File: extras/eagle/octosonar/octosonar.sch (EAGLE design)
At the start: 21 parts, among them IC1 PCF8574TW, IC2 74HC125D, IC3 74HC125D

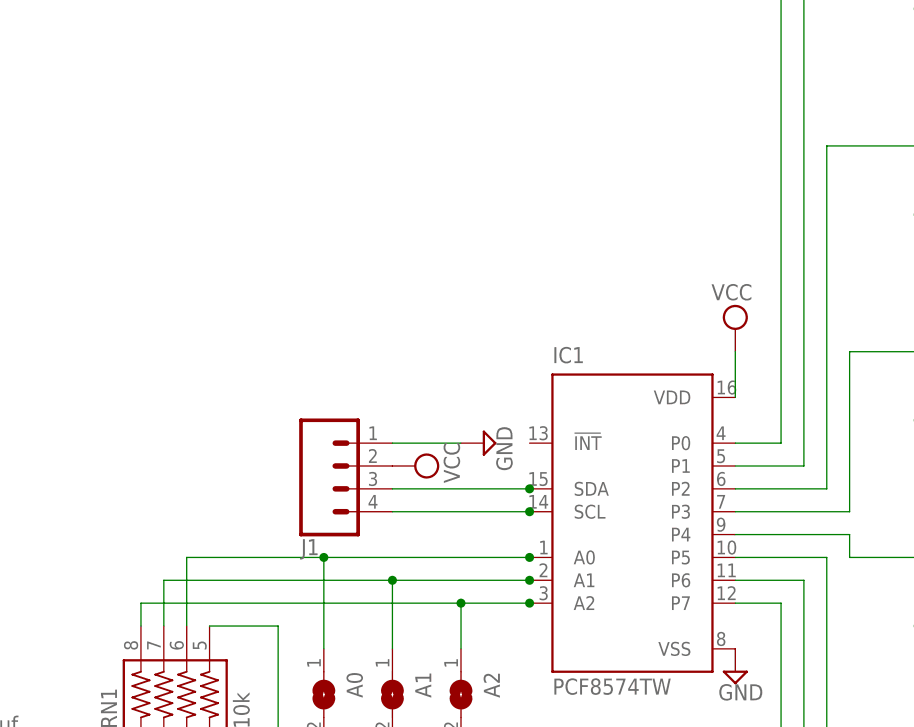
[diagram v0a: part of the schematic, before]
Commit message: octosonar board 2.1 first pass
input pins on grid
add i2c pullups
silkscreen rework
full re-route
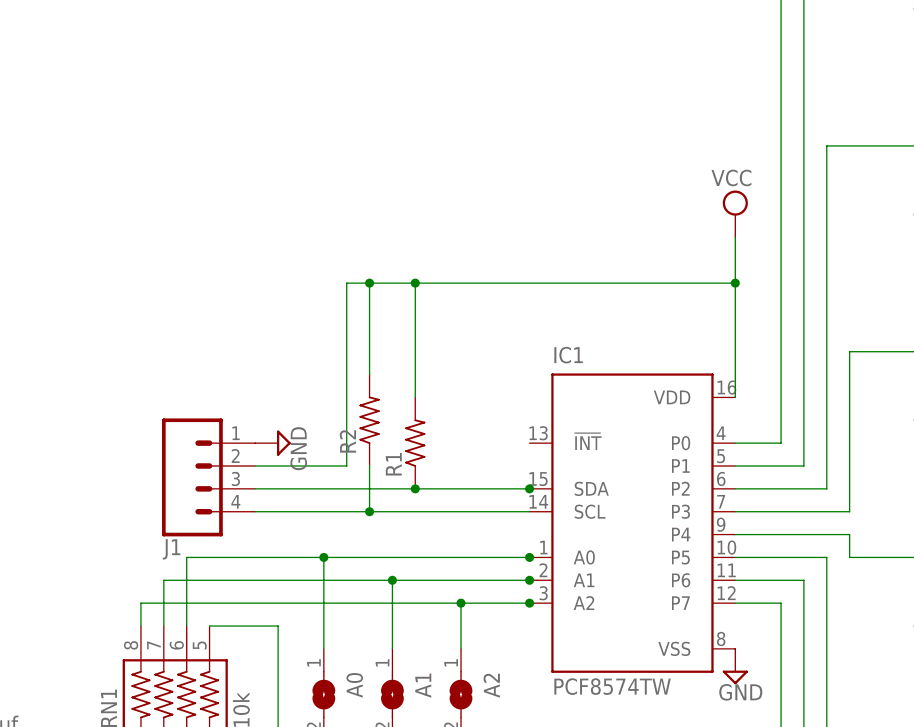
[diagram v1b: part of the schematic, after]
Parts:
- added R1, R2: (no value), rcl:R-US_0204/2V
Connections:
- net N$21: now also R2.1
- net N$22: now also R1.1
- net VCC: now also R1.2, R2.2
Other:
- moved on the sheet: J1
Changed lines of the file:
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@@
 <?xml version="1.0" encoding="utf-8"?>
 <!DOCTYPE eagle SYSTEM "eagle.dtd">
-<eagle version="8.2.0">
+<eagle version="8.2.1">
 <drawing>
 <settings>
@@
 <layers>
 <layer number="1" name="Top" color="4" fill="1" visible="no" active="no"/>
+<layer number="2" name="Route2" color="1" fill="3" visible="no" active="no"/>
+<layer number="15" name="Route15" color="4" fill="6" visible="no" active="no"/>
 <layer number="16" name="Bottom" color="1" fill="1" visible="no" active="no"/>
 <layer number="17" name="Pads" color="2" fill="1" visible="no" active="no"/>
@@
 <parts>
 <part name="IC2" library="74xx-eu" deviceset="74*125" device="D" technology="HC"/>
-<part name="IC3" library="74xx-eu" deviceset="74*125" device="D" technology="HC"/>
+<part name="IC3" library="74xx-eu" library_urn="urn:adsk.eagle:library:85" deviceset="74*125" device="D" technology="HC"/>
 <part name="S0" library="SparkFun-Connectors" deviceset="CONN_04" device="POLAR_LOCK" value="0"/>
 <part name="S1" library="SparkFun-Connectors" deviceset="CONN_04" device="POLAR_LOCK" value="1"/>
@@
 <part name="SUPPLY18" library="supply2" deviceset="VCC" device=""/>
 <part name="J1" library="SparkFun-Connectors" deviceset="CONN_04" device="POLAR_LOCK"/>
-<part name="SUPPLY21" library="supply2" deviceset="VCC" device=""/>
 <part name="SUPPLY22" library="supply2" deviceset="GND" device=""/>
 <part name="J2" library="SparkFun-Connectors" deviceset="CONN_02" device="POLAR_LOCK"/>
@@
 <part name="VCC1" library="supply2" deviceset="VCC" device=""/>
 <part name="SUPPLY25" library="supply2" deviceset="GND" device=""/>
+<part name="R1" library="rcl" library_urn="urn:adsk.eagle:library:334" deviceset="R-US_" device="0204/2V"/>
+<part name="R2" library="rcl" library_urn="urn:adsk.eagle:library:334" deviceset="R-US_" device="0204/2V"/>
 </parts>
 <sheets>
@@
 <instance part="SUPPLY14" gate="GND" x="111.76" y="-101.6"/>
 <instance part="SUPPLY18" gate="G$1" x="5.08" y="-55.88" rot="R180"/>
-<instance part="J1" gate="G$1" x="0" y="-10.16" rot="MR180"/>
-<instance part="SUPPLY21" gate="G$1" x="7.62" y="-10.16" rot="MR90"/>
-<instance part="SUPPLY22" gate="GND" x="15.24" y="-7.62" rot="MR270"/>
+<instance part="J1" gate="G$1" x="-15.24" y="-10.16" rot="MR180"/>
+<instance part="SUPPLY22" gate="GND" x="-7.62" y="-7.62" rot="MR270"/>
 <instance part="J2" gate="G$1" x="33.02" y="-50.8"/>
 <instance part="IC1" gate="G$1" x="30.48" y="-15.24"/>
 <instance part="SUPPLY23" gate="GND" x="43.18" y="-33.02"/>
-<instance part="VCC" gate="G$1" x="43.18" y="5.08" rot="MR0"/>
+<instance part="VCC" gate="G$1" x="43.18" y="17.78" rot="MR0"/>
 <instance part="SUPPLY5" gate="+5V" x="111.76" y="71.12"/>
 <instance part="SUPPLY7" gate="+5V" x="111.76" y="48.26"/>
@@
 <instance part="VCC1" gate="G$1" x="-55.88" y="-22.86" rot="MR0"/>
 <instance part="SUPPLY25" gate="GND" x="-55.88" y="-48.26"/>
+<instance part="R1" gate="G$1" x="7.62" y="-7.62" rot="R90"/>
+<instance part="R2" gate="G$1" x="2.54" y="-5.08" rot="R90"/>
 </instances>
 <busses>
@@
 <pinref part="J1" gate="G$1" pin="1"/>
 <pinref part="SUPPLY22" gate="GND" pin="GND"/>
-<wire x1="12.7" y1="-7.62" x2="5.08" y2="-7.62" width="0.1524" layer="91"/>
 </segment>
 <segment>
@@
 <net name="VCC" class="0">
 <segment>
-<pinref part="J1" gate="G$1" pin="2"/>
-<pinref part="SUPPLY21" gate="G$1" pin="VCC"/>
-</segment>
-<segment>
 <pinref part="IC1" gate="G$1" pin="VDD"/>
 <pinref part="VCC" gate="G$1" pin="VCC"/>
-<wire x1="43.18" y1="2.54" x2="43.18" y2="-2.54" width="0.1524" layer="91"/>
+<wire x1="43.18" y1="15.24" x2="43.18" y2="10.16" width="0.1524" layer="91"/>
+<wire x1="43.18" y1="10.16" x2="43.18" y2="-2.54" width="0.1524" layer="91"/>
+<wire x1="43.18" y1="10.16" x2="7.62" y2="10.16" width="0.1524" layer="91"/>
+<junction x="43.18" y="10.16"/>
+<wire x1="7.62" y1="10.16" x2="2.54" y2="10.16" width="0.1524" layer="91"/>
+<wire x1="2.54" y1="10.16" x2="0" y2="10.16" width="0.1524" layer="91"/>
+<wire x1="0" y1="10.16" x2="0" y2="-10.16" width="0.1524" layer="91"/>
+<pinref part="J1" gate="G$1" pin="2"/>
+<wire x1="0" y1="-10.16" x2="-10.16" y2="-10.16" width="0.1524" layer="91"/>
+<pinref part="R2" gate="G$1" pin="2"/>
+<wire x1="2.54" y1="0" x2="2.54" y2="10.16" width="0.1524" layer="91"/>
+<junction x="2.54" y="10.16"/>
+<pinref part="R1" gate="G$1" pin="2"/>
+<wire x1="7.62" y1="-2.54" x2="7.62" y2="10.16" width="0.1524" layer="91"/>
+<junction x="7.62" y="10.16"/>
 </segment>
 <segment>
@@
 <segment>
 <pinref part="J1" gate="G$1" pin="4"/>
-<wire x1="20.32" y1="-15.24" x2="5.08" y2="-15.24" width="0.1524" layer="91"/>
 <pinref part="IC1" gate="G$1" pin="SCL"/>
-<junction x="20.32" y="-15.24"/>
+<pinref part="R2" gate="G$1" pin="1"/>
+<wire x1="-10.16" y1="-15.24" x2="2.54" y2="-15.24" width="0.1524" layer="91"/>
+<wire x1="2.54" y1="-15.24" x2="20.32" y2="-15.24" width="0.1524" layer="91"/>
+<wire x1="2.54" y1="-10.16" x2="2.54" y2="-15.24" width="0.1524" layer="91"/>
+<junction x="2.54" y="-15.24"/>
 </segment>
 </net>
@@
 <segment>
 <pinref part="J1" gate="G$1" pin="3"/>
-<wire x1="20.32" y1="-12.7" x2="5.08" y2="-12.7" width="0.1524" layer="91"/>
+<wire x1="20.32" y1="-12.7" x2="7.62" y2="-12.7" width="0.1524" layer="91"/>
 <pinref part="IC1" gate="G$1" pin="SDA"/>
 <junction x="20.32" y="-12.7"/>
+<pinref part="R1" gate="G$1" pin="1"/>
+<wire x1="7.62" y1="-12.7" x2="-10.16" y2="-12.7" width="0.1524" layer="91"/>
+<junction x="7.62" y="-12.7"/>
 </segment>
 </net>
@@
 </schematic>
 </drawing>
+<compatibility>
+<note version="8.2" severity="warning">
+Since Version 8.2, Eagle supports online libraries. The ids
+of those online libraries will not be understood (or retained)
+with this version.
+</note>
+</compatibility>
 </eagle>
